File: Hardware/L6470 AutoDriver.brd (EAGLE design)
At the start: 73.7 x 49.5 mm, 37 parts, among them U1 L6470

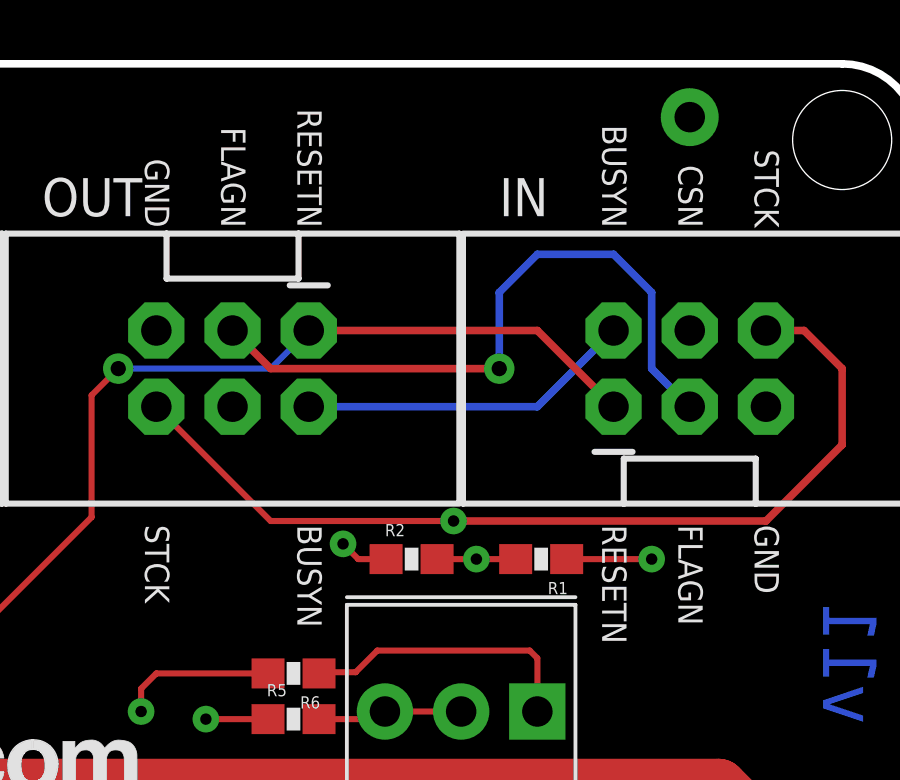
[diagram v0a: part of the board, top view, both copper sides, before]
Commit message: Connect CSN to CSN_OUT, minor fixes
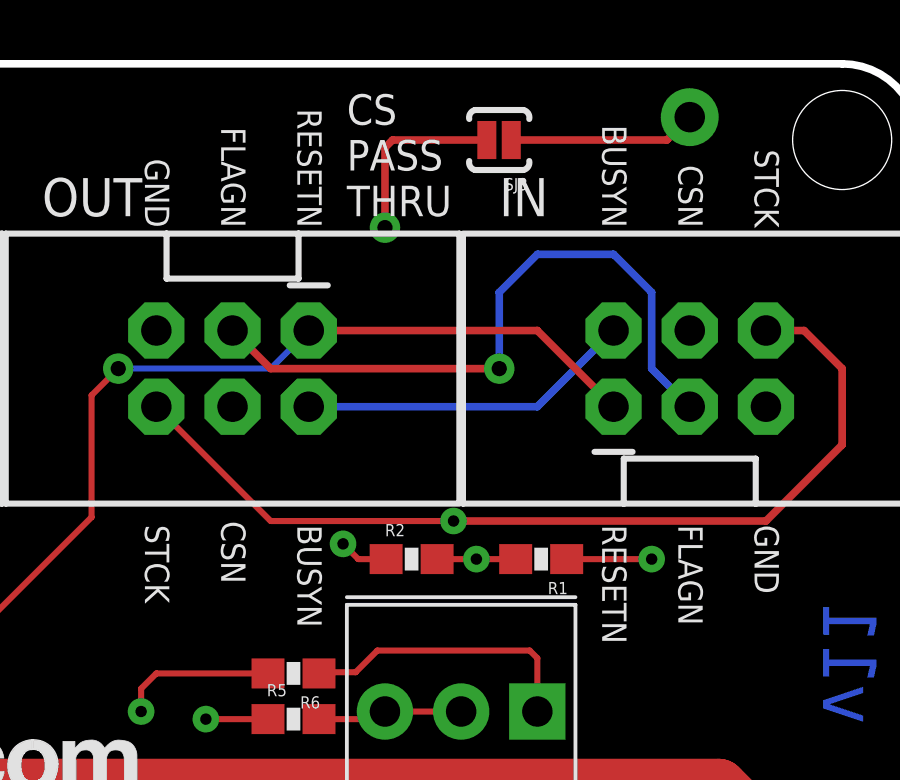
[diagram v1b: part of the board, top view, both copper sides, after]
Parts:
- added SJ3: JUMPER-PAD-2-NC_BY_PASTE, SparkFun-Passives:PAD-JUMPER-2-NC_BY_PASTE_YES_SILK
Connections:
- new net CSN_OUT: JP3.4, SJ3.2
- net CSN: now also SJ3.1
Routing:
- net CSN_OUT: track 0.00 -> 20.5 mm, vias 0 -> 1
- net CSN: track 58.2 -> 64.4 mm
- net ADC: track 42.7 -> 43.8 mm
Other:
- board text added: "CS PASS THRU"

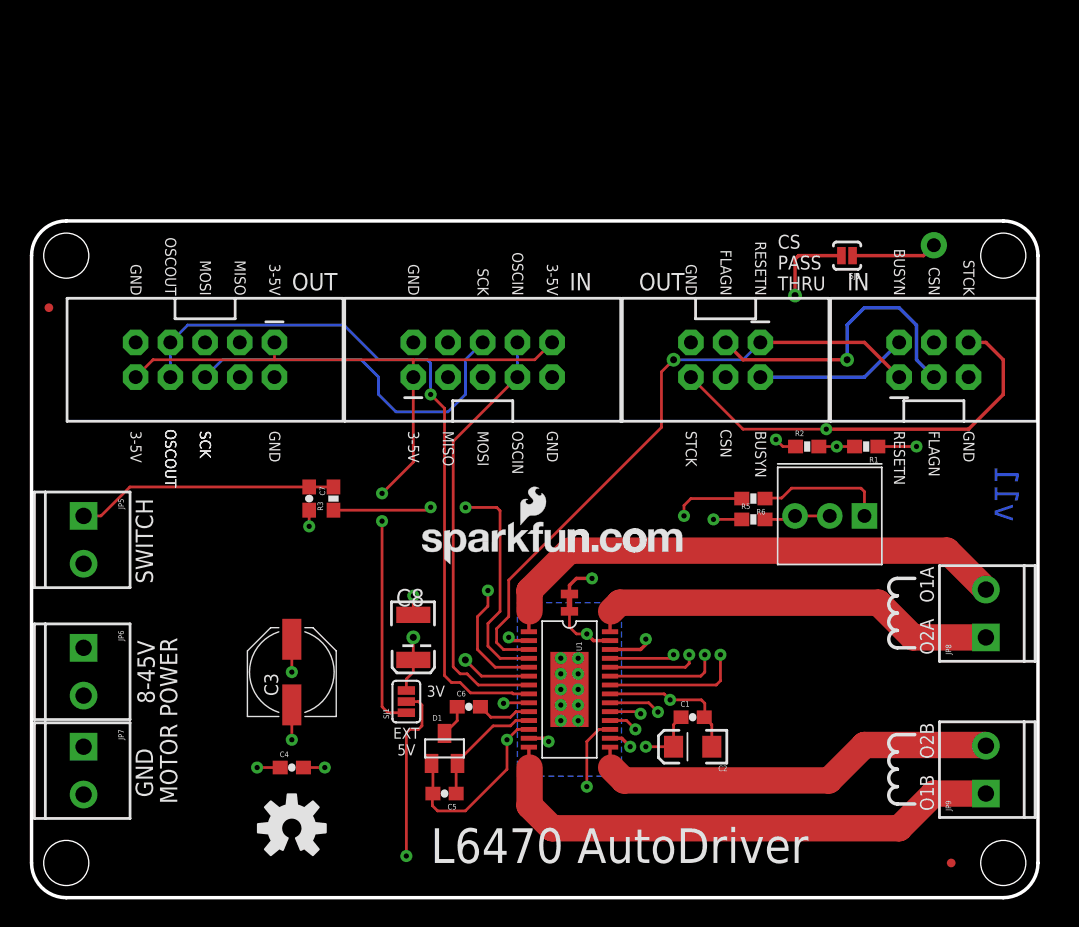
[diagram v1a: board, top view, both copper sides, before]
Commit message: Making changes suggest by Pete L
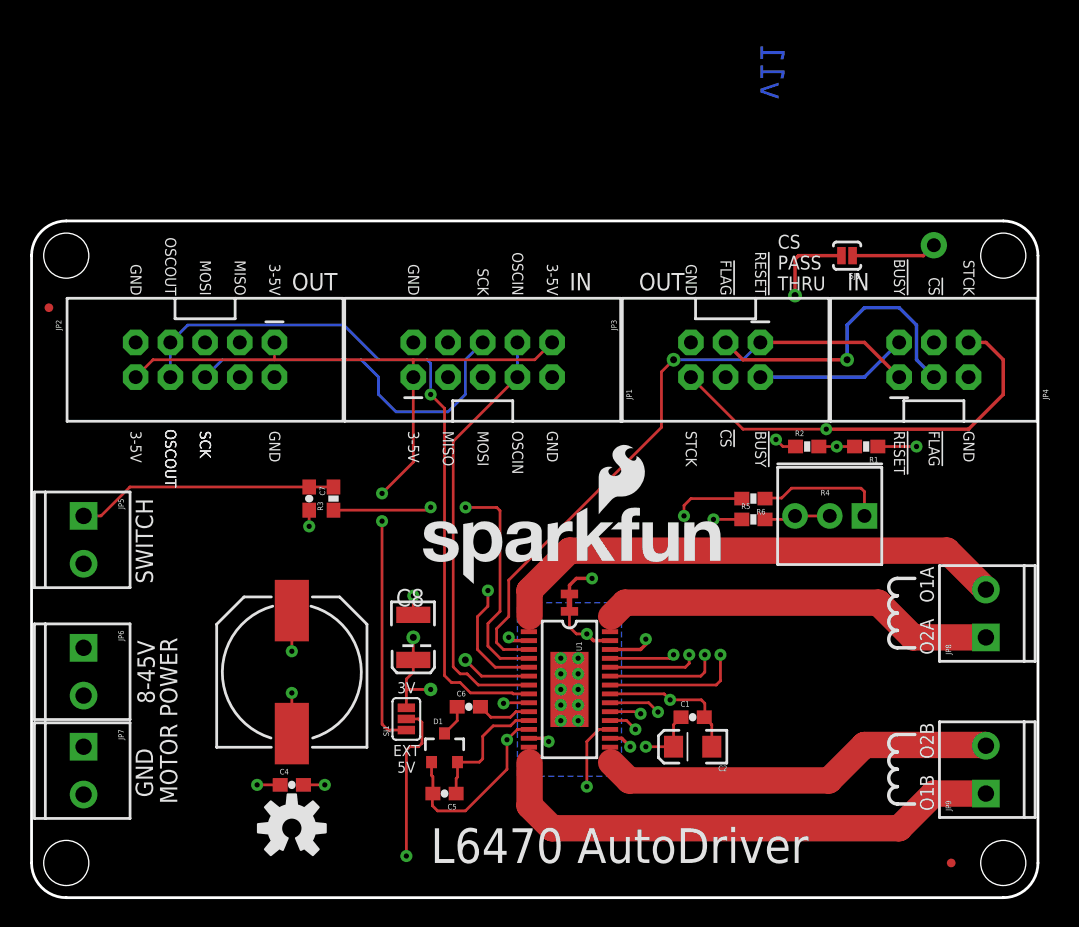
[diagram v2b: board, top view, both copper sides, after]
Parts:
- added TP1: TEST-POINTTP_15TH_THRU, SparkFun-Passives:TP_15TH
- C3: device SparkFun-Capacitors:PANASONIC_D -> SparkFun-Capacitors:NIC_10X10.5_CAP
- D1: device SparkFun-DiscreteSemi:SOT23 -> SparkFun-DiscreteSemi:SOT23-3
- FRAME1: value FRAME-LETTER -> (none)
- LOGO2: value LOGO-SFENEW -> SFE_LOGO_NAME_FLAME.2_INCH; device SparkFun:SFE-NEW-WEBLOGO -> SparkFun-Aesthetics:SFE_LOGO_NAME_FLAME_.2
- R4: device SparkFun:3362U -> SparkFun-Electromechanical:3362U
- moved U$4 11.7 mm to (3.81, -3.81)
- moved FRAME1 8.03 mm to (3.81, -12.7)
- moved LOGO2 1.65 mm to (27.9, 22.9)
- moved SJ1 1.27 mm to (27.4, 13.1)
- moved C4 1.27 mm to (19.1, 8.26)
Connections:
- net 3.3V: now also TP1.P$1
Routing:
- net 3.3V: track 13.7 -> 16.8 mm
- net N$9: track 9.00 -> 10.5 mm
- net VLOGIC: track 92.1 -> 90.8 mm
- net 5V: track 61.1 -> 62.4 mm
- net VS: track 40.0 -> 40.7 mm
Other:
- board text added: "!BUSY"
- board text added: "!CS"
- board text added: "!FLAG"
- board text added: "!RESET"
- board text removed: "CSN"
- board text removed: "FLAGN"
- board text removed: "M.Hord"
- board text removed: "RESETN"
- board text removed: "v11"

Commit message: Fixed more feedback from Pete after 1st proto cam failure
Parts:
- added JP10: (no value), SparkFun-Connectors:1X01
- moved U$4 54.7 mm to (58.4, -7.62)
- moved FRAME1 21.8 mm to (21.6, -25.4)
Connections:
- net CSN: now also JP10.1
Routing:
- net CSN: track 64.4 -> 63.3 mm, vias 2 -> 1
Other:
- board text added: "(typical)"
- board text added: "1"
- board text added: "2"
- board text added: "3"
- board text added: "4"
- board text added: "Mike Hord"
- board text added: "dimensions given in inches"
- board text added: "v11"

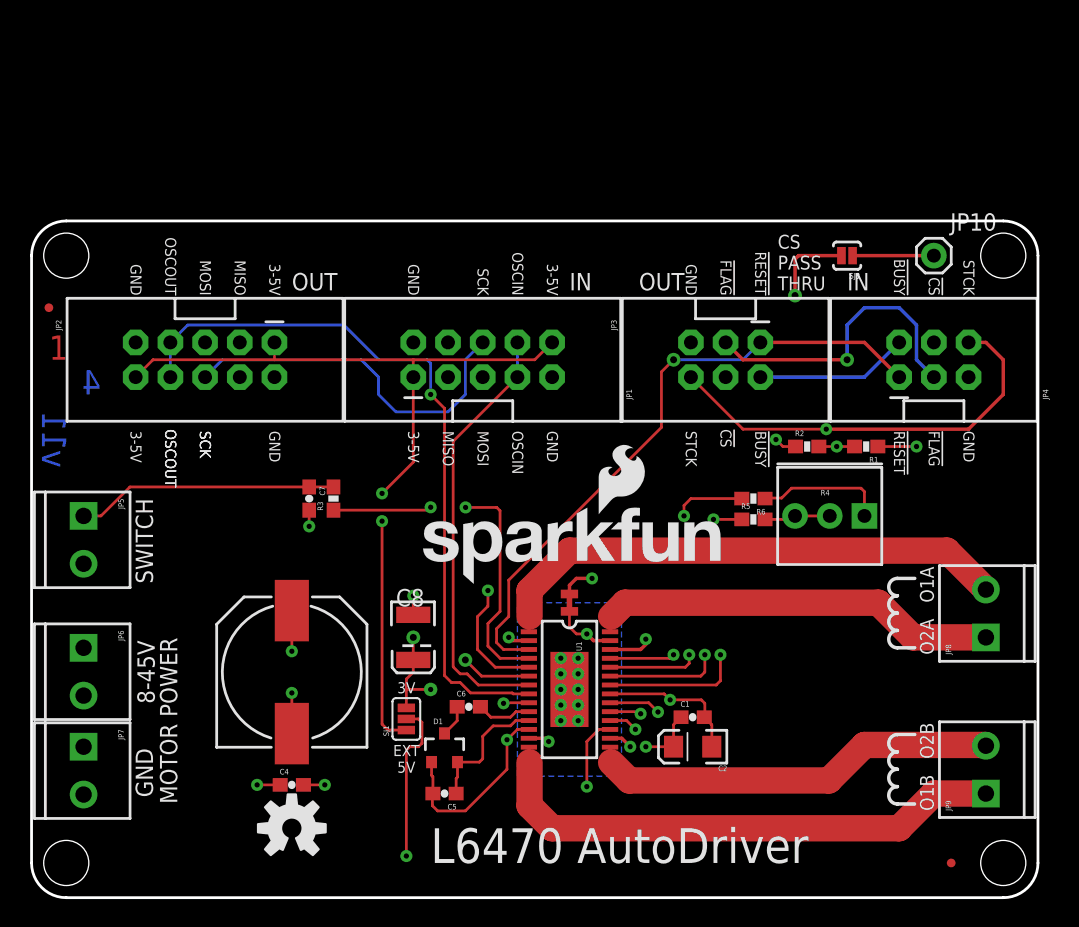
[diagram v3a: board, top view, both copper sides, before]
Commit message: Significant changes from customer feedback:  - now more daisy chainable  - labels changed to make more sense  - Change C5 to 220nF
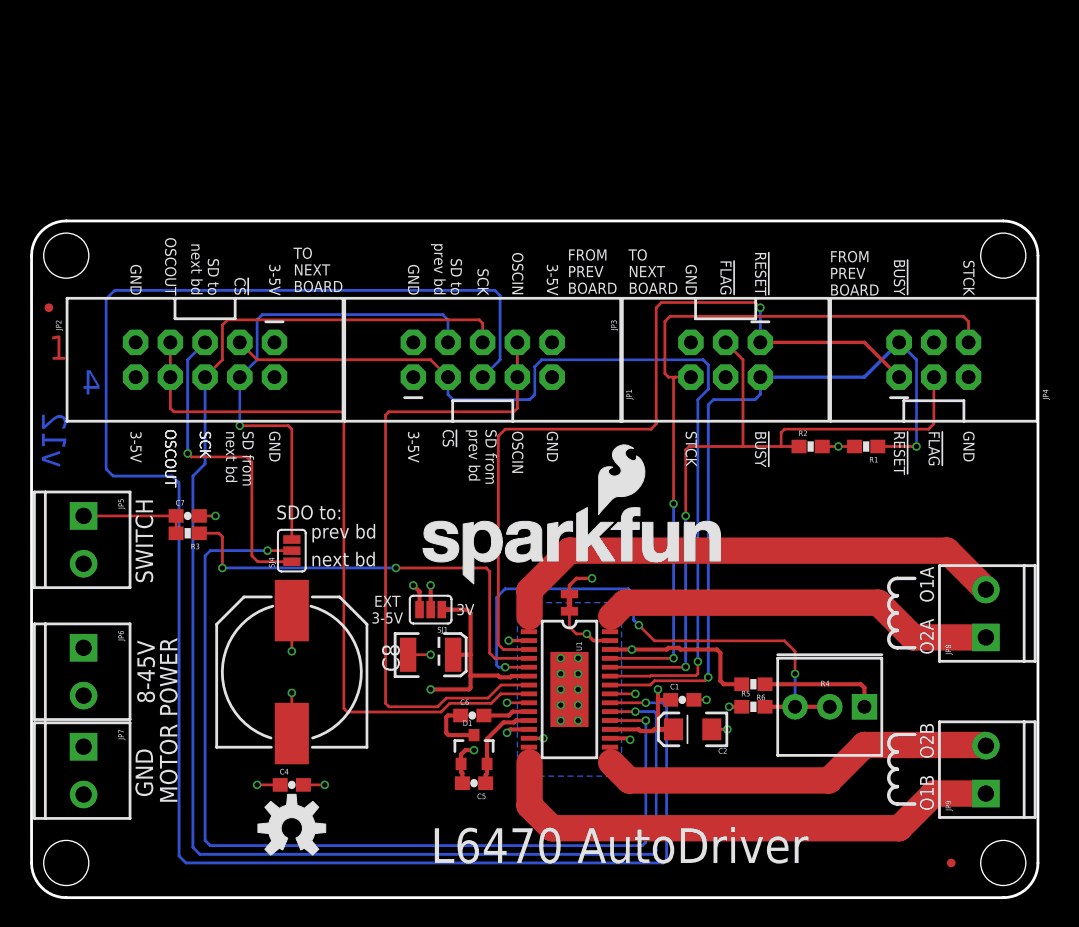
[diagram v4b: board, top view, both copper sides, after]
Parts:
- removed JP10: (no value), SparkFun-Connectors:1X01
- removed SJ3: JUMPER-PAD-2-NC_BY_PASTE, SparkFun-Passives:PAD-JUMPER-2-NC_BY_PASTE_YES_SILK
- added SJ4: JUMPER-PAD-3-2OF3_NC_BY_PASTE, SparkFun-Passives:PAD-JUMPER-3-2OF3_NC_BY_PASTE_YES_SILK_FULL_BOX
- FRAME1: value (none) -> FRAME-LETTER
- SJ1: value (none) -> JUMPER-PAD-3-2OF3_NC_BY_PASTE; device SparkFun-Passives:SJ_3_PASTE1&2 -> SparkFun-Passives:PAD-JUMPER-3-2OF3_NC_BY_PASTE_YES_SILK_FULL_BOX
- moved R4 14.0 mm to (61.0, 16.5)
- moved R5 13.7 mm to (52.8, 14.0)
- moved R6 13.6 mm to (52.8, 15.6)
- moved R3 11.0 mm to (11.4, 26.7), turned to 180 degrees
- moved C7 8.98 mm to (11.4, 27.9), turned to 0 degrees
- moved SJ1 8.20 mm to (29.2, 21.1), turned to 180 degrees
- moved C5 2.29 mm to (32.4, 8.38)
- moved D1 2.16 mm to (32.4, 10.8)
- moved C8 1.80 mm to (29.2, 17.8), turned to 0 degrees
- moved C1 1.48 mm to (47.6, 14.5)
- moved C2 1.27 mm to (48.4, 12.3)
- moved C6 0.68 mm to (32.3, 13.3)
- moved R2 0.25 mm to (57.0, 33.0)
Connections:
- net N$5 renamed SWITCH_SIG
- net N$6 renamed SWITCH_INPUT
- net N$7 renamed V_CP
- net N$8 renamed CP_HIGH
- net N$9 renamed V_BOOT
- removed net CSN_OUT: JP3.4, SJ3.2
- removed net MISO: JP1.3, JP2.3, U1.18
- removed net MOSI: JP1.5, JP2.5, U1.20
- new net D_RETURN: JP1.4, JP2.4, SJ4.3
- new net SDI: JP1.5, U1.20
- new net SDO: SJ4.2, U1.18
- new net SDO_DOWNSTREAM: JP2.5, SJ4.1
- net 3.3V: now also SJ1.1; no longer SJ1.3
- net 5V: now also SJ1.3; no longer SJ1.1
- net CSN: now also JP1.3, JP2.3; no longer JP10.1, JP4.4, SJ3.1
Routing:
- net SDI: track 0.00 -> 132.7 mm, vias 0 -> 1
- net MOSI: track 77.4 -> 0.00 mm, vias 1 -> 0
- net SDO: track 0.00 -> 71.4 mm, vias 0 -> 2
- net MISO: track 62.0 -> 0.00 mm, vias 1 -> 0
- net D_RETURN: track 0.00 -> 36.2 mm, vias 0 -> 1
- net VLOGIC: track 90.8 -> 62.9 mm, vias 4 -> 3
- net SDO_DOWNSTREAM: track 0.00 -> 23.6 mm, vias 0 -> 1
- net FLAGN: track 75.4 -> 54.4 mm, vias 3 -> 2
- net CSN_OUT: track 20.5 -> 0.00 mm, vias 1 -> 0
- net SCK: track 87.5 -> 107.5 mm
- net VS: track 40.7 -> 24.6 mm
- net STCK: track 71.2 -> 55.2 mm
- net OSCIN: track 31.8 -> 47.0 mm
- net RESETN: track 46.7 -> 59.8 mm
- net SWITCH_INPUT: track 19.2 -> 8.04 mm
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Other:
- board text added: "EXT 3-5V"
- board text added: "FROM PREV BOARD"
- board text added: "SD from next bd"
- board text added: "SD from prev bd"
- board text added: "SD to next bd"
- board text added: "SD to prev bd"
- board text added: "SDO to:"
- board text added: "TO NEXT BOARD"
- board text added: "next bd"
- board text added: "prev bd"
- board text added: "v12"
- board text removed: "CS PASS THRU"
- board text removed: "EXT 5V"
- board text removed: "IN"
- board text removed: "OUT"
- board text removed: "v11"

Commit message: Changes from customer feedback:  - now easier to daisy chain!  - labels make more sense in light of daisy chaining  - change C5 to 220nF
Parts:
- C5: value 10nF -> 0.22uF
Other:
- board text added: "M3/4-40"
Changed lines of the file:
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@@
 <text x="53.721" y="42.037" size="0.8128" layer="22" font="vector" ratio="15" rot="SMR270" align="bottom-right">!RESET</text>
 <text x="63.881" y="42.037" size="0.8128" layer="22" font="vector" ratio="15" rot="SMR270" align="bottom-right">BUSYN</text>
-<text x="66.421" y="42.037" size="0.8128" layer="22" font="vector" ratio="15" rot="SMR270" align="bottom-right">!CS</text>
 <text x="68.961" y="42.037" size="0.8128" layer="22" font="vector" ratio="15" rot="SMR270" align="bottom-right">STCK</text>
 <text x="8.001" y="41.91" size="0.8128" layer="22" font="vector" ratio="15" rot="SMR270" align="bottom-right">GND</text>
@@
 PREV
 BOARD</text>
+<dimension x1="2.54" y1="2.54" x2="-7.62" y2="-2.54" x3="-13.97" y3="-2.54" textsize="1.778" textratio="15" layer="47" dtype="leader" unit="inch"/>
+<text x="-25.4" y="-3.81" size="1.778" layer="47" font="vector" ratio="15">M3/4-40</text>
 </plain>
 <attributes>
@@
 <attribute name="VALUE" value="10nF" x="32.258" y="13.335" size="1.778" layer="27" display="off"/>
 </element>
-<element name="C5" library="SparkFun-Capacitors" package="0603-CAP" value="10nF" x="32.385" y="8.382" rot="R180">
-<attribute name="PROD_ID" value="CAP-00867" x="32.385" y="8.382" size="1.778" layer="27" rot="R180" display="off"/>
-<attribute name="VALUE" value="10nF" x="32.385" y="8.382" size="1.778" layer="27" rot="R180" display="off"/>
+<element name="C5" library="SparkFun-Capacitors" package="0603-CAP" value="0.22uF" x="32.385" y="8.382" rot="R180">
+<attribute name="PROD_ID" value="CAP-09885" x="32.385" y="8.382" size="1.778" layer="27" rot="R180" display="off"/>
+<attribute name="VALUE" value="0.22uF" x="32.385" y="8.382" size="1.778" layer="27" rot="R180" display="off"/>
 </element>
 <element name="C4" library="SparkFun-Capacitors" package="0603-CAP" value="0.22uF" x="19.05" y="8.255">

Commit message: Final file changes from revision
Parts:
- moved R3 0.25 mm to (11.4, 26.4)
- renumbered SJ4 to SJ3
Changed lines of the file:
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@@
 <?xml version="1.0" encoding="utf-8"?>
 <!DOCTYPE eagle SYSTEM "eagle.dtd">
-<eagle version="7.3.0">
+<eagle version="7.5.0">
 <drawing>
 <settings>
@@
 <layer number="47" name="Measures" color="7" fill="1" visible="no" active="yes"/>
 <layer number="51" name="tDocu" color="6" fill="1" visible="yes" active="yes"/>
-<layer number="52" name="bDocu" color="7" fill="1" visible="no" active="no"/>
+<layer number="52" name="bDocu" color="7" fill="1" visible="no" active="yes"/>
 <layer number="3" name="Route3" color="4" fill="3" visible="no" active="no"/>
 <layer number="4" name="Route4" color="1" fill="4" visible="no" active="no"/>
@@
 <attribute name="VALUE" value="10nF" x="11.43" y="27.94" size="1.778" layer="27" display="off"/>
 </element>
-<element name="R3" library="SparkFun-Resistors" package="0603-RES" value="100" x="11.43" y="26.67" rot="R180">
-<attribute name="PROD_ID" value="RES-07863" x="11.43" y="26.67" size="1.778" layer="27" rot="R180" display="off"/>
-<attribute name="VALUE" value="100" x="11.43" y="26.67" size="1.778" layer="27" rot="R180" display="off"/>
+<element name="R3" library="SparkFun-Resistors" package="0603-RES" value="100" x="11.43" y="26.416" rot="R180">
+<attribute name="PROD_ID" value="RES-07863" x="11.43" y="26.416" size="1.778" layer="27" rot="R180" display="off"/>
+<attribute name="VALUE" value="100" x="11.43" y="26.416" size="1.778" layer="27" rot="R180" display="off"/>
 </element>
 <element name="R4" library="SparkFun-Electromechanical" package="3362U" value="200k" x="60.96" y="16.51" rot="R180"/>
@@
 <element name="TP1" library="SparkFun-Passives" package="TP_15TH" value="TEST-POINTTP_15TH_THRU" x="29.21" y="15.24"/>
 <element name="FRAME1" library="SparkFun-Aesthetics" package="CREATIVE_COMMONS" value="FRAME-LETTER" x="21.59" y="-25.4" smashed="yes"/>
-<element name="SJ4" library="SparkFun-Passives" package="PAD-JUMPER-3-2OF3_NC_BY_PASTE_YES_SILK_FULL_BOX" value="JUMPER-PAD-3-2OF3_NC_BY_PASTE" x="19.05" y="25.4" rot="R90"/>
+<element name="SJ3" library="SparkFun-Passives" package="PAD-JUMPER-3-2OF3_NC_BY_PASTE_YES_SILK_FULL_BOX" value="JUMPER-PAD-3-2OF3_NC_BY_PASTE" x="19.05" y="25.4" rot="R90"/>
 </elements>
 <signals>
@@
 <wire x1="26.67" y1="24.13" x2="13.97" y2="24.13" width="0.2032" layer="16"/>
 <via x="13.97" y="24.13" extent="1-16" drill="0.381"/>
-<wire x1="13.97" y1="24.13" x2="13.97" y2="26.416" width="0.2032" layer="1"/>
-<wire x1="13.97" y1="26.416" x2="13.716" y2="26.67" width="0.2032" layer="1"/>
-<wire x1="13.716" y1="26.67" x2="12.28" y2="26.67" width="0.2032" layer="1"/>
+<wire x1="13.97" y1="24.13" x2="13.97" y2="26.162" width="0.2032" layer="1"/>
+<wire x1="13.97" y1="26.162" x2="13.716" y2="26.416" width="0.2032" layer="1"/>
+<wire x1="13.716" y1="26.416" x2="12.28" y2="26.416" width="0.2032" layer="1"/>
 </signal>
 <signal name="SWITCH_INPUT">
@@
 <contactref element="C7" pad="1"/>
 <contactref element="JP5" pad="1"/>
-<wire x1="10.58" y1="26.67" x2="10.58" y2="27.94" width="0.2032" layer="1"/>
+<wire x1="10.58" y1="26.416" x2="10.58" y2="27.94" width="0.2032" layer="1"/>
 <wire x1="3.81" y1="27.94" x2="10.58" y2="27.94" width="0.2032" layer="1"/>
 </signal>
@@
 <contactref element="JP1" pad="4"/>
 <contactref element="JP2" pad="4"/>
-<contactref element="SJ4" pad="3"/>
+<contactref element="SJ3" pad="3"/>
 <wire x1="19.05" y1="26.2128" x2="19.05" y2="34.29" width="0.2032" layer="1"/>
 <wire x1="19.05" y1="34.29" x2="18.796" y2="34.544" width="0.2032" layer="1"/>
@@
 <signal name="SDO">
 <contactref element="U1" pad="18"/>
-<contactref element="SJ4" pad="2"/>
+<contactref element="SJ3" pad="2"/>
 <wire x1="42.34" y1="12.965" x2="44.958" y2="12.965" width="0.2032" layer="1"/>
 <via x="44.958" y="12.965" extent="1-16" drill="0.381"/>
@@
 <signal name="SDO_DOWNSTREAM">
 <contactref element="JP2" pad="5"/>
-<contactref element="SJ4" pad="1"/>
+<contactref element="SJ3" pad="1"/>
 <wire x1="19.05" y1="24.5872" x2="16.5608" y2="24.5872" width="0.2032" layer="1"/>
 <wire x1="16.5608" y1="24.5872" x2="16.129" y2="25.019" width="0.2032" layer="1"/>
